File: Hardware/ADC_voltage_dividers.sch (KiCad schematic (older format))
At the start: 8 parts

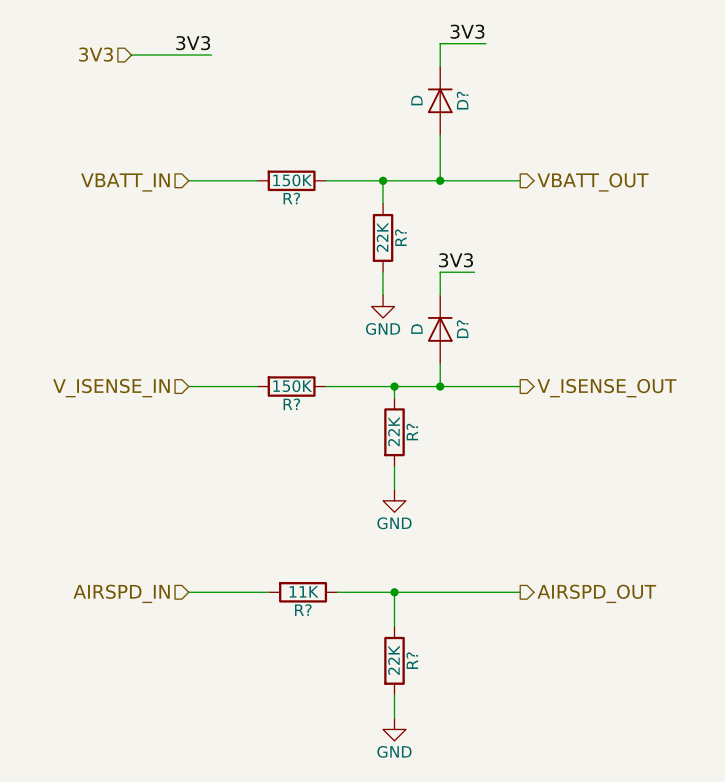
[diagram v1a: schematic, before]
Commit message: Generated netlist and board outline
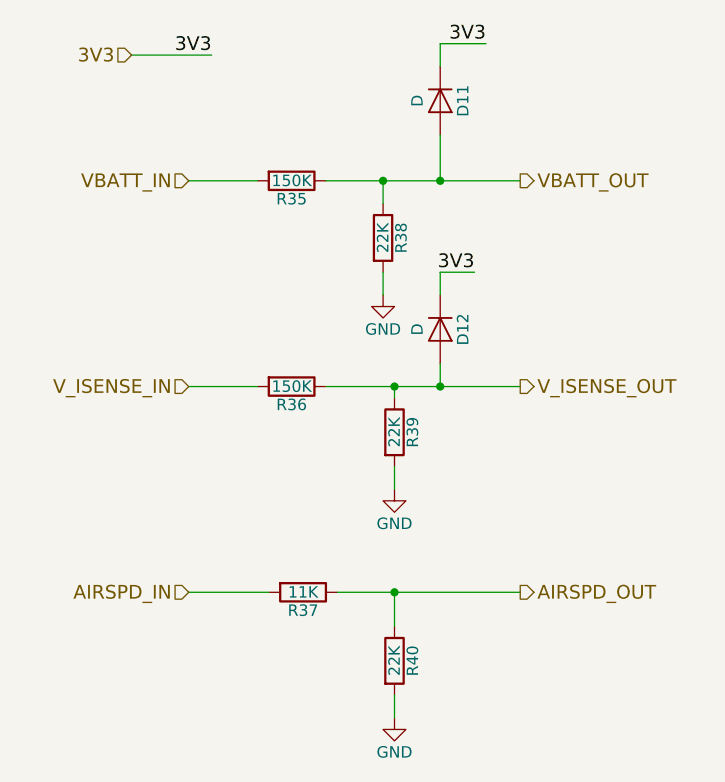
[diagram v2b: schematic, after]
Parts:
- gave numbers to parts that had none: 8
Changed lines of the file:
@@
 $EndDescr
 $Comp
-L power:GND #PWR?
+L power:GND #PWR042
 U 1 1 596892B4
 P 3850 3150
-F 0 "#PWR?" H 3850 2900 50  0001 C CNN
+F 0 "#PWR042" H 3850 2900 50  0001 C CNN
 F 1 "GND" H 3850 3000 50  0000 C CNN
 F 2 "" H 3850 3150 50  0001 C CNN
@@
 $EndComp
 $Comp
-L Device:D D?
+L Device:D D11
 U 1 1 596892D3
 P 4050 1450
-F 0 "D?" H 4050 1550 50  0000 C CNN
+F 0 "D11" H 4050 1550 50  0000 C CNN
 F 1 "D" H 4050 1350 50  0000 C CNN
 F 2 "Diodes_SMD:D_SMA_Handsoldering" H 4050 1450 50  0001 C CNN
@@
 $EndComp
 $Comp
-L Device:D D?
+L Device:D D12
 U 1 1 596892DB
 P 4050 2450
-F 0 "D?" H 4050 2550 50  0000 C CNN
+F 0 "D12" H 4050 2550 50  0000 C CNN
 F 1 "D" H 4050 2350 50  0000 C CNN
 F 2 "Diodes_SMD:D_SMA_Handsoldering" H 4050 2450 50  0001 C CNN
@@
 	3850 3050 3850 3150
 $Comp
-L Device:R R?
+L Device:R R39
 U 1 1 596892FC
 P 3850 2900
-F 0 "R?" V 3930 2900 50  0000 C CNN
+F 0 "R39" V 3930 2900 50  0000 C CNN
 F 1 "22K" V 3850 2900 50  0000 C CNN
 F 2 "Resistors_SMD:R_0603_HandSoldering" V 3780 2900 50  0001 C CNN
@@
 $EndComp
 $Comp
-L Device:R R?
+L Device:R R36
 U 1 1 59689304
 P 3400 2700
-F 0 "R?" V 3480 2700 50  0000 C CNN
+F 0 "R36" V 3480 2700 50  0000 C CNN
 F 1 "150K" V 3400 2700 50  0000 C CNN
 F 2 "Resistors_SMD:R_0603_HandSoldering" V 3330 2700 50  0001 C CNN
@@
 Connection ~ 3850 2700
 $Comp
-L power:GND #PWR?
+L power:GND #PWR041
 U 1 1 59689CAD
 P 3800 2300
-F 0 "#PWR?" H 3800 2050 50  0001 C CNN
+F 0 "#PWR041" H 3800 2050 50  0001 C CNN
 F 1 "GND" H 3800 2150 50  0000 C CNN
 F 2 "" H 3800 2300 50  0001 C CNN
@@
 	3800 2200 3800 2300
 $Comp
-L Device:R R?
+L Device:R R38
 U 1 1 59689CB5
 P 3800 2050
-F 0 "R?" V 3880 2050 50  0000 C CNN
+F 0 "R38" V 3880 2050 50  0000 C CNN
 F 1 "22K" V 3800 2050 50  0000 C CNN
 F 2 "Resistors_SMD:R_0603_HandSoldering" V 3730 2050 50  0001 C CNN
@@
 AIRSPD_OUT
 $Comp
-L power:GND #PWR?
+L power:GND #PWR043
 U 1 1 59689D8B
 P 3850 4150
-F 0 "#PWR?" H 3850 3900 50  0001 C CNN
+F 0 "#PWR043" H 3850 3900 50  0001 C CNN
 F 1 "GND" H 3850 4000 50  0000 C CNN
 F 2 "" H 3850 4150 50  0001 C CNN
@@
 	3850 4050 3850 4150
 $Comp
-L Device:R R?
+L Device:R R40
 U 1 1 59689D93
 P 3850 3900
-F 0 "R?" V 3930 3900 50  0000 C CNN
+F 0 "R40" V 3930 3900 50  0000 C CNN
 F 1 "22K" V 3850 3900 50  0000 C CNN
 F 2 "Resistors_SMD:R_0603_HandSoldering" V 3780 3900 50  0001 C CNN
@@
 	3600 3600 3850 3600
 $Comp
-L Device:R R?
+L Device:R R37
 U 1 1 59689DC9
 P 3450 3600
-F 0 "R?" V 3530 3600 50  0000 C CNN
+F 0 "R37" V 3530 3600 50  0000 C CNN
 F 1 "11K" V 3450 3600 50  0000 C CNN
 F 2 "Resistors_SMD:R_0603_HandSoldering" V 3380 3600 50  0001 C CNN
@@
 	3300 3600 2950 3600
 $Comp
-L Device:R R?
+L Device:R R35
 U 1 1 599BFDE6
 P 3400 1800
-F 0 "R?" V 3480 1800 50  0000 C CNN
+F 0 "R35" V 3480 1800 50  0000 C CNN
 F 1 "150K" V 3400 1800 50  0000 C CNN
 F 2 "Resistors_SMD:R_0603_HandSoldering" V 3330 1800 50  0001 C CNN

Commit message: Initial Routing of Zeropilot Rev1
This is the initial routing of the board. It needs to be cleaned up slightly, but library references are screwed up so they will be fixed first.
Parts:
- D11, D12: footprint Diodes_SMD:D_SMA_Handsoldering -> Diodes_SMD:D_PowerDI-123; part_num DIOD-005 -> DIOD-007
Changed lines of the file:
@@
 EESchema Schematic File Version 4
-LIBS:ZeroPilot-cache
-EELAYER 26 0
+EELAYER 29 0
 EELAYER END
 $Descr A4 11693 8268
@@
 F 0 "D11" H 4050 1550 50  0000 C CNN
 F 1 "D" H 4050 1350 50  0000 C CNN
-F 2 "Diodes_SMD:D_SMA_Handsoldering" H 4050 1450 50  0001 C CNN
-F 3 "https://www.diodes.com/assets/Datasheets/ds16003.pdf" H 4050 1450 50  0001 C CNN
-F 4 "DIOD-005" H 4050 1450 60  0001 C CNN "part_num"
+F 2 "Diodes_SMD:D_PowerDI-123" H 4050 1450 50  0001 C CNN
+F 3 "https://www.diodes.com/assets/Datasheets/ds30492.pdf" H 4050 1450 50  0001 C CNN
+F 4 "DIOD-007" H 4050 1450 60  0001 C CNN "part_num"
 	1    4050 1450
 	0    1    1    0
@@
 F 0 "D12" H 4050 2550 50  0000 C CNN
 F 1 "D" H 4050 2350 50  0000 C CNN
-F 2 "Diodes_SMD:D_SMA_Handsoldering" H 4050 2450 50  0001 C CNN
-F 3 "https://www.diodes.com/assets/Datasheets/ds16003.pdf" H 4050 2450 50  0001 C CNN
-F 4 "DIOD-005" H 4050 2450 60  0001 C CNN "part_num"
+F 2 "Diodes_SMD:D_PowerDI-123" H 4050 2450 50  0001 C CNN
+F 3 "https://www.diodes.com/assets/Datasheets/ds30492.pdf" H 4050 2450 50  0001 C CNN
+F 4 "DIOD-007" H 4050 2450 60  0001 C CNN "part_num"
 	1    4050 2450
 	0    1    1    0

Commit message: Updated Footprints
Updated the footprints to 5.1, added 3D models to all components.
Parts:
- D11, D12: footprint Diodes_SMD:D_PowerDI-123 -> Diode_SMD:D_PowerDI-123
- R35, R36, R37, R38, R39, R40: footprint Resistors_SMD:R_0603_HandSoldering -> Resistor_SMD:R_0603_1608Metric_Pad1.05x0.95mm_HandSolder
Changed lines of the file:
@@
 EESchema Schematic File Version 4
+LIBS:ZeroPilot-cache
 EELAYER 29 0
 EELAYER END
@@
 F 0 "D11" H 4050 1550 50  0000 C CNN
 F 1 "D" H 4050 1350 50  0000 C CNN
-F 2 "Diodes_SMD:D_PowerDI-123" H 4050 1450 50  0001 C CNN
+F 2 "Diode_SMD:D_PowerDI-123" H 4050 1450 50  0001 C CNN
 F 3 "https://www.diodes.com/assets/Datasheets/ds30492.pdf" H 4050 1450 50  0001 C CNN
 F 4 "DIOD-007" H 4050 1450 60  0001 C CNN "part_num"
@@
 F 0 "D12" H 4050 2550 50  0000 C CNN
 F 1 "D" H 4050 2350 50  0000 C CNN
-F 2 "Diodes_SMD:D_PowerDI-123" H 4050 2450 50  0001 C CNN
+F 2 "Diode_SMD:D_PowerDI-123" H 4050 2450 50  0001 C CNN
 F 3 "https://www.diodes.com/assets/Datasheets/ds30492.pdf" H 4050 2450 50  0001 C CNN
 F 4 "DIOD-007" H 4050 2450 60  0001 C CNN "part_num"
@@
 F 0 "R39" V 3930 2900 50  0000 C CNN
 F 1 "22K" V 3850 2900 50  0000 C CNN
-F 2 "Resistors_SMD:R_0603_HandSoldering" V 3780 2900 50  0001 C CNN
+F 2 "Resistor_SMD:R_0603_1608Metric_Pad1.05x0.95mm_HandSolder" V 3780 2900 50  0001 C CNN
 F 3 "http://www.yageo.com/documents/recent/PYu-RC_Group_51_RoHS_L_10.pdf" H 3850 2900 50  0001 C CNN
 F 4 "RESS-002" V 3850 2900 60  0001 C CNN "part_num"
@@
 F 0 "R36" V 3480 2700 50  0000 C CNN
 F 1 "150K" V 3400 2700 50  0000 C CNN
-F 2 "Resistors_SMD:R_0603_HandSoldering" V 3330 2700 50  0001 C CNN
+F 2 "Resistor_SMD:R_0603_1608Metric_Pad1.05x0.95mm_HandSolder" V 3330 2700 50  0001 C CNN
 F 3 "http://www.yageo.com/documents/recent/PYu-RC_Group_51_RoHS_L_10.pdf" H 3400 2700 50  0001 C CNN
 F 4 "RESS-007" V 3400 2700 60  0001 C CNN "part_num"
@@
 F 0 "R38" V 3880 2050 50  0000 C CNN
 F 1 "22K" V 3800 2050 50  0000 C CNN
-F 2 "Resistors_SMD:R_0603_HandSoldering" V 3730 2050 50  0001 C CNN
+F 2 "Resistor_SMD:R_0603_1608Metric_Pad1.05x0.95mm_HandSolder" V 3730 2050 50  0001 C CNN
 F 3 "http://www.yageo.com/documents/recent/PYu-RC_Group_51_RoHS_L_10.pdf" H 3800 2050 50  0001 C CNN
 F 4 "RESS-002" V 3800 2050 60  0001 C CNN "part_num"
@@
 F 0 "R40" V 3930 3900 50  0000 C CNN
 F 1 "22K" V 3850 3900 50  0000 C CNN
-F 2 "Resistors_SMD:R_0603_HandSoldering" V 3780 3900 50  0001 C CNN
+F 2 "Resistor_SMD:R_0603_1608Metric_Pad1.05x0.95mm_HandSolder" V 3780 3900 50  0001 C CNN
 F 3 "http://www.yageo.com/documents/recent/PYu-RC_Group_51_RoHS_L_10.pdf" H 3850 3900 50  0001 C CNN
 F 4 "RESS-002" V 3850 3900 60  0001 C CNN "part_num"
@@
 F 0 "R37" V 3530 3600 50  0000 C CNN
 F 1 "11K" V 3450 3600 50  0000 C CNN
-F 2 "Resistors_SMD:R_0603_HandSoldering" V 3380 3600 50  0001 C CNN
+F 2 "Resistor_SMD:R_0603_1608Metric_Pad1.05x0.95mm_HandSolder" V 3380 3600 50  0001 C CNN
 F 3 "http://www.yageo.com/documents/recent/PYu-RC_Group_51_RoHS_L_10.pdf" H 3450 3600 50  0001 C CNN
 F 4 "RESS-004" V 3450 3600 60  0001 C CNN "part_num"
@@
 F 0 "R35" V 3480 1800 50  0000 C CNN
 F 1 "150K" V 3400 1800 50  0000 C CNN
-F 2 "Resistors_SMD:R_0603_HandSoldering" V 3330 1800 50  0001 C CNN
+F 2 "Resistor_SMD:R_0603_1608Metric_Pad1.05x0.95mm_HandSolder" V 3330 1800 50  0001 C CNN
 F 3 "http://www.yageo.com/documents/recent/PYu-RC_Group_51_RoHS_L_10.pdf" H 3400 1800 50  0001 C CNN
 F 4 "RESS-007" V 3400 1800 60  0001 C CNN "part_num"

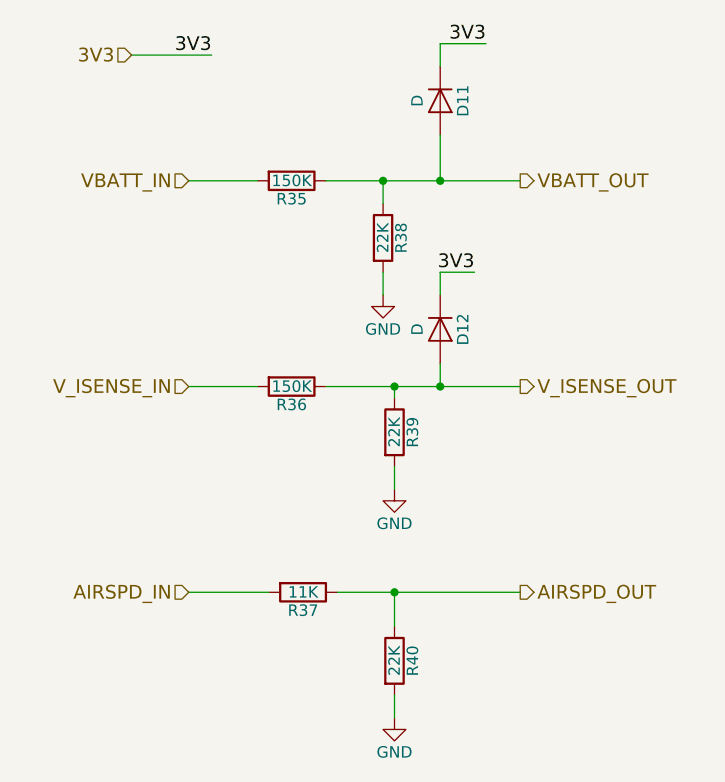
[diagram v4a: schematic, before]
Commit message: HW Bootcamp for Zeropilot R1
Changed the board to R1.
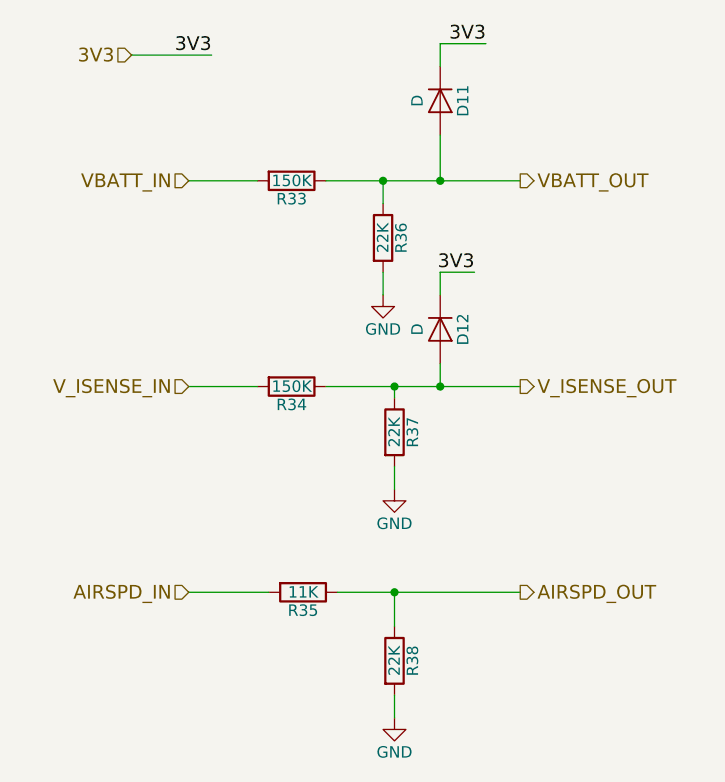
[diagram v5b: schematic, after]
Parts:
- renumbered R35 to R33, R36 to R34, R37 to R35, R38 to R36, R39 to R37, R40 to R38
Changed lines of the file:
@@
 EESchema Schematic File Version 4
-LIBS:ZeroPilot-cache
 EELAYER 29 0
 EELAYER END
@@
 $EndDescr
 $Comp
-L power:GND #PWR042
+L power:GND #PWR037
 U 1 1 596892B4
 P 3850 3150
-F 0 "#PWR042" H 3850 2900 50  0001 C CNN
+F 0 "#PWR037" H 3850 2900 50  0001 C CNN
 F 1 "GND" H 3850 3000 50  0000 C CNN
 F 2 "" H 3850 3150 50  0001 C CNN
@@
 	3850 3050 3850 3150
 $Comp
-L Device:R R39
+L Device:R R37
 U 1 1 596892FC
 P 3850 2900
-F 0 "R39" V 3930 2900 50  0000 C CNN
+F 0 "R37" V 3930 2900 50  0000 C CNN
 F 1 "22K" V 3850 2900 50  0000 C CNN
 F 2 "Resistor_SMD:R_0603_1608Metric_Pad1.05x0.95mm_HandSolder" V 3780 2900 50  0001 C CNN
@@
 $EndComp
 $Comp
-L Device:R R36
+L Device:R R34
 U 1 1 59689304
 P 3400 2700
-F 0 "R36" V 3480 2700 50  0000 C CNN
+F 0 "R34" V 3480 2700 50  0000 C CNN
 F 1 "150K" V 3400 2700 50  0000 C CNN
 F 2 "Resistor_SMD:R_0603_1608Metric_Pad1.05x0.95mm_HandSolder" V 3330 2700 50  0001 C CNN
@@
 Connection ~ 3850 2700
 $Comp
-L power:GND #PWR041
+L power:GND #PWR036
 U 1 1 59689CAD
 P 3800 2300
-F 0 "#PWR041" H 3800 2050 50  0001 C CNN
+F 0 "#PWR036" H 3800 2050 50  0001 C CNN
 F 1 "GND" H 3800 2150 50  0000 C CNN
 F 2 "" H 3800 2300 50  0001 C CNN
@@
 	3800 2200 3800 2300
 $Comp
-L Device:R R38
+L Device:R R36
 U 1 1 59689CB5
 P 3800 2050
-F 0 "R38" V 3880 2050 50  0000 C CNN
+F 0 "R36" V 3880 2050 50  0000 C CNN
 F 1 "22K" V 3800 2050 50  0000 C CNN
 F 2 "Resistor_SMD:R_0603_1608Metric_Pad1.05x0.95mm_HandSolder" V 3730 2050 50  0001 C CNN
@@
 AIRSPD_OUT
 $Comp
-L power:GND #PWR043
+L power:GND #PWR038
 U 1 1 59689D8B
 P 3850 4150
-F 0 "#PWR043" H 3850 3900 50  0001 C CNN
+F 0 "#PWR038" H 3850 3900 50  0001 C CNN
 F 1 "GND" H 3850 4000 50  0000 C CNN
 F 2 "" H 3850 4150 50  0001 C CNN
@@
 	3850 4050 3850 4150
 $Comp
-L Device:R R40
+L Device:R R38
 U 1 1 59689D93
 P 3850 3900
-F 0 "R40" V 3930 3900 50  0000 C CNN
+F 0 "R38" V 3930 3900 50  0000 C CNN
 F 1 "22K" V 3850 3900 50  0000 C CNN
 F 2 "Resistor_SMD:R_0603_1608Metric_Pad1.05x0.95mm_HandSolder" V 3780 3900 50  0001 C CNN
@@
 	3600 3600 3850 3600
 $Comp
-L Device:R R37
+L Device:R R35
 U 1 1 59689DC9
 P 3450 3600
-F 0 "R37" V 3530 3600 50  0000 C CNN
+F 0 "R35" V 3530 3600 50  0000 C CNN
 F 1 "11K" V 3450 3600 50  0000 C CNN
 F 2 "Resistor_SMD:R_0603_1608Metric_Pad1.05x0.95mm_HandSolder" V 3380 3600 50  0001 C CNN
@@
 	3300 3600 2950 3600
 $Comp
-L Device:R R35
+L Device:R R33
 U 1 1 599BFDE6
 P 3400 1800
-F 0 "R35" V 3480 1800 50  0000 C CNN
+F 0 "R33" V 3480 1800 50  0000 C CNN
 F 1 "150K" V 3400 1800 50  0000 C CNN
 F 2 "Resistor_SMD:R_0603_1608Metric_Pad1.05x0.95mm_HandSolder" V 3330 1800 50  0001 C CNN
